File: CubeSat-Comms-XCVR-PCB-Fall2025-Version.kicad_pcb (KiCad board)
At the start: 4 copper layers, 93.9 x 97.3 mm, 70 parts, among them J1 Conn_01x02_Pin, J2 Conn_01x02_Pin, J3 Conn_Coaxial, J4 Conn_01x12_Pin, U1 CC1101RGP, U2 SKY65366-21, U3 PE4251MLI-Z, U4 NCP186AMX390TAG, Y1 NX3225GA-26MHZ-TI

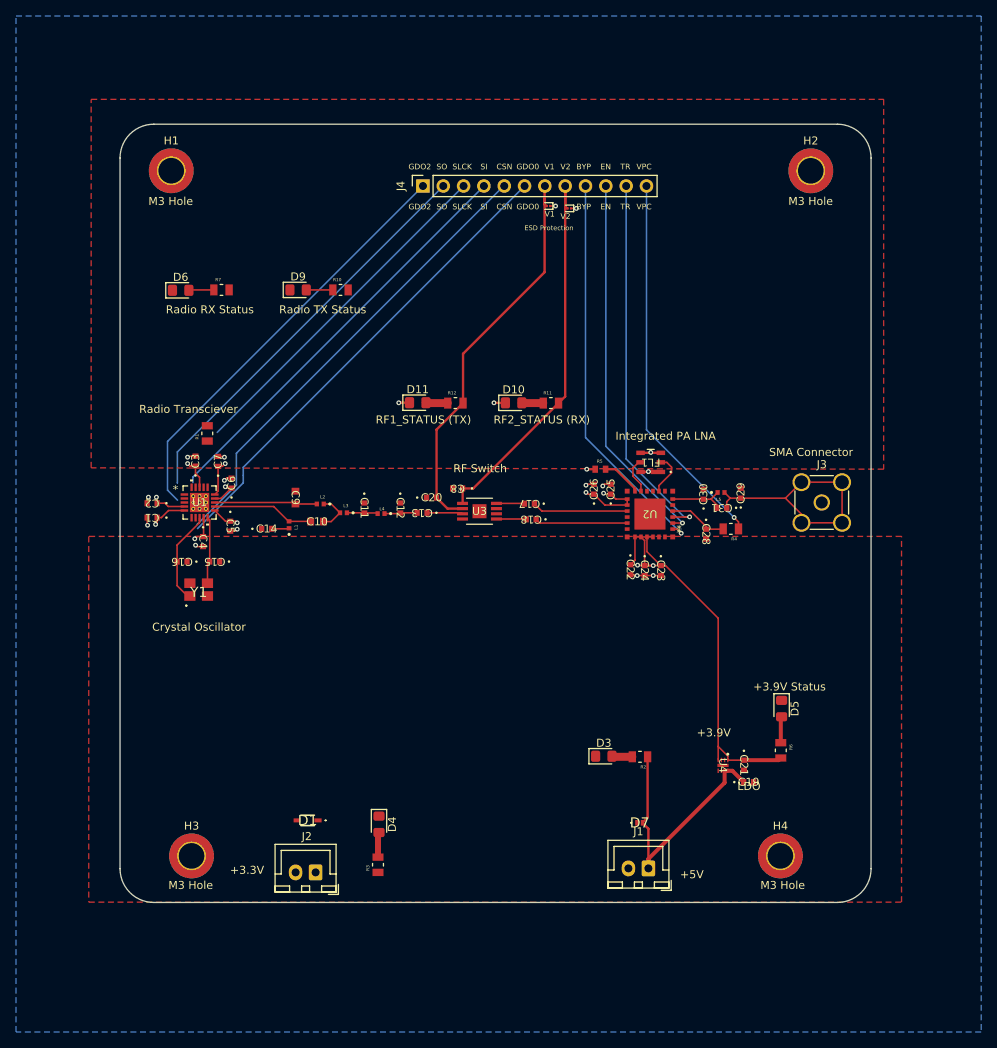
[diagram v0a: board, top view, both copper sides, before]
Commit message: pcb edits: sticking vias, trace routing...
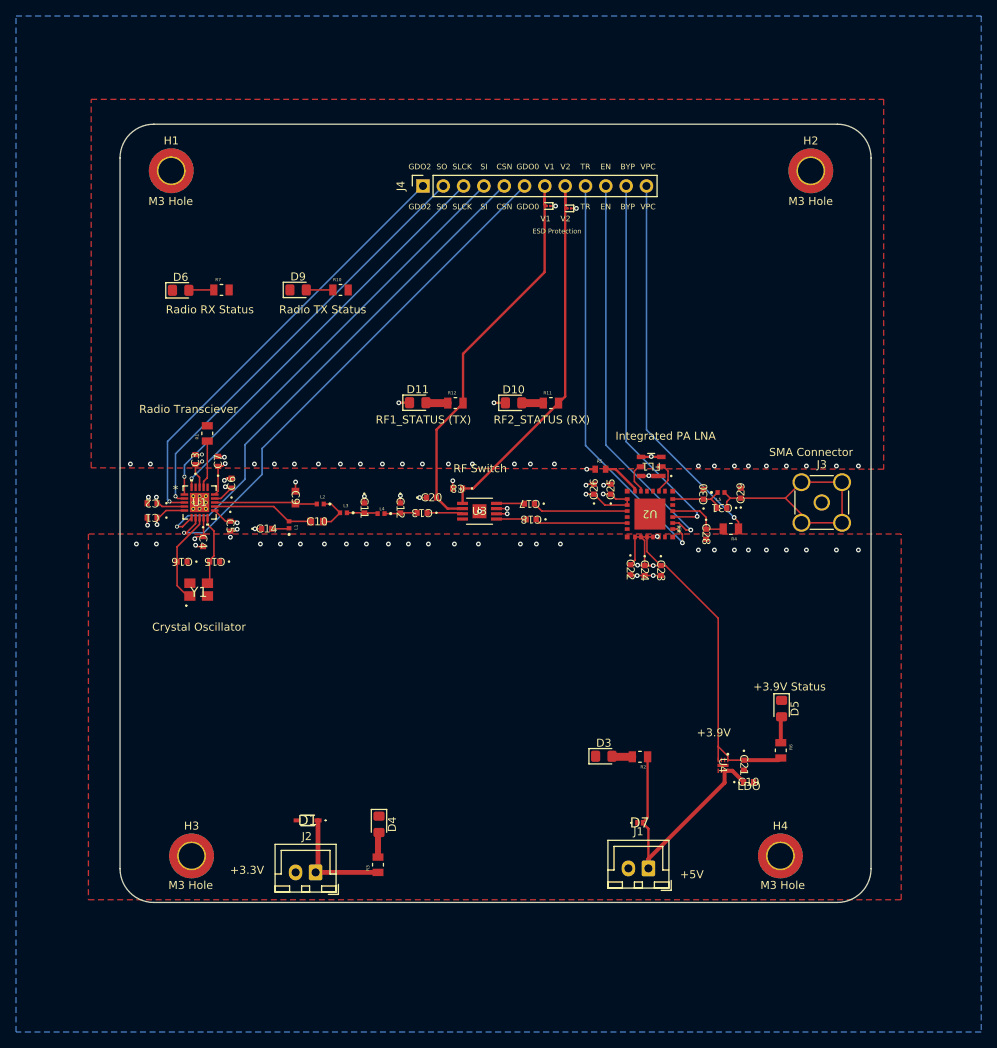
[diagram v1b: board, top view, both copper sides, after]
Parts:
- moved FL1 0.51 mm to (123.8, 88.1)
- moved C3 0.20 mm to (66.9, 87.2)
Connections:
- J4 pad 5: CSN -> GD00
- J4 pad 6: GD00 -> CSN
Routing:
- net +3.3V: track 38.0 -> 52.7 mm
- net SCLK: track 43.6 -> 53.0 mm, vias 0 -> 1
- net GND: track 22.6 -> 30.6 mm, vias 18 -> 79
- net CSN: track 58.3 -> 65.1 mm, vias 0 -> 1
- net Net-(U1-RBIAS): track 0.00 -> 5.98 mm
- net GD00: track 59.8 -> 63.4 mm, vias 0 -> 1
- net SO: track 50.9 -> 53.9 mm, vias 0 -> 1
- net EN: track 47.3 -> 50.0 mm
- net TR: track 49.6 -> 52.2 mm
- net GD02: track 53.0 -> 54.7 mm, vias 0 -> 1
- net SAW_IN: track 5.25 -> 4.05 mm
- net BYP: track 47.2 -> 48.1 mm
- net Net-(U2-VPC): track 7.46 -> 8.14 mm
- net SI: track 52.1 -> 52.8 mm, vias 0 -> 1
- net SAW_OUT: track 4.56 -> 3.92 mm

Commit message: revised board clearance rules, drc, routing, placements. TODO = redundant xcvr, impedance matching
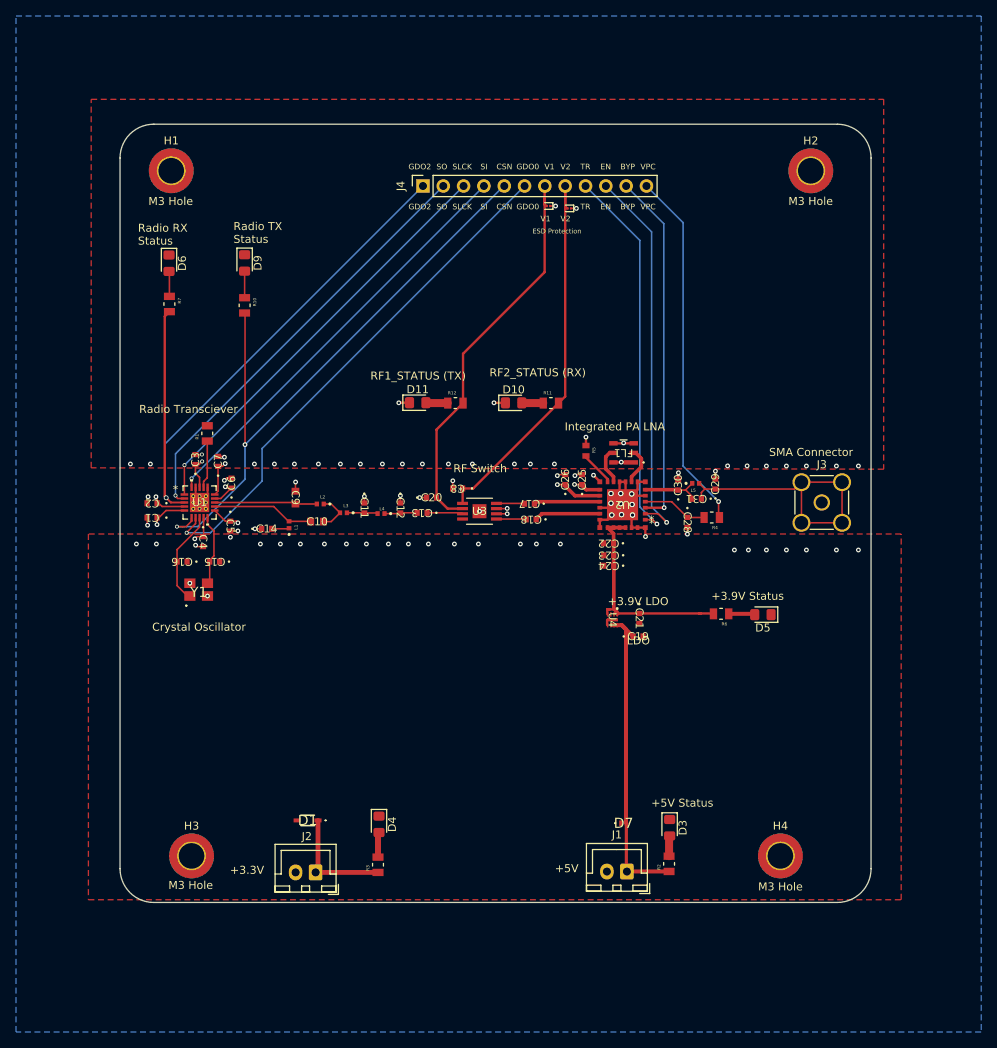
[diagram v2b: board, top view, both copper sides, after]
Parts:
- moved C19 22.9 mm to (122.2, 109.3)
- moved U4 22.9 mm to (119.0, 107.2)
- moved C21 22.5 mm to (122.4, 107.1)
- moved R6 18.6 mm to (132.6, 106.5), turned to 180 degrees
- moved R2 13.9 mm to (126.1, 137.7), turned to 90 degrees
- moved R10 12.1 mm to (73.0, 67.9), turned to -90 degrees
- moved D3 12.1 mm to (126.2, 133.2), turned to -90 degrees
- moved D5 12.0 mm to (137.8, 106.6), turned to 180 degrees
- moved D9 7.49 mm to (73.0, 62.6), turned to -90 degrees
- moved C23 6.79 mm to (118.5, 99.2), turned to 180 degrees
- moved R7 6.74 mm to (63.6, 67.8), turned to -90 degrees
- moved C24 4.52 mm to (118.5, 100.5), turned to 180 degrees
- moved C22 4.28 mm to (118.5, 97.7), turned to 180 degrees
- moved FL1 3.85 mm to (120.4, 86.4)
- moved C25 3.78 mm to (115.2, 89.7)
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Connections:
- U1 pad V: (no net) -> GND
- U4 pad 2: unconnected-(U4-OUT-Pad2) -> +3.9V
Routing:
- net GND: track 30.6 -> 64.9 mm, vias 79 -> 88
- net +3.9V: track 55.5 -> 28.8 mm, vias 2 -> 0
- net GD02: track 54.7 -> 78.5 mm
- net GD00: track 63.4 -> 80.2 mm, vias 1 -> 2
- net +5V: track 34.4 -> 39.6 mm
- net TR: track 52.2 -> 47.6 mm
- net Net-(J3-Ext): track 31.3 -> 35.1 mm
- net RX0: track 12.0 -> 8.27 mm
- net BYP: track 48.1 -> 44.5 mm
- net TX: track 11.6 -> 8.24 mm
- net VPC: track 47.6 -> 45.2 mm
- net EN: track 50.0 -> 48.3 mm
- net SAW_OUT: track 3.92 -> 4.69 mm
- net Net-(U2-RBIAS): track 5.00 -> 4.35 mm
- net SAW_IN: track 4.05 -> 4.67 mm
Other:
- rule pad_to_mask_clearance: 0 -> 0.2
- board text added: "+3.9V LDO"
- board text added: "+5V Status"
- board text removed: "+3.9V"

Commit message: editted silk screen and note on schematic about via tenting for CC1101 epad vias
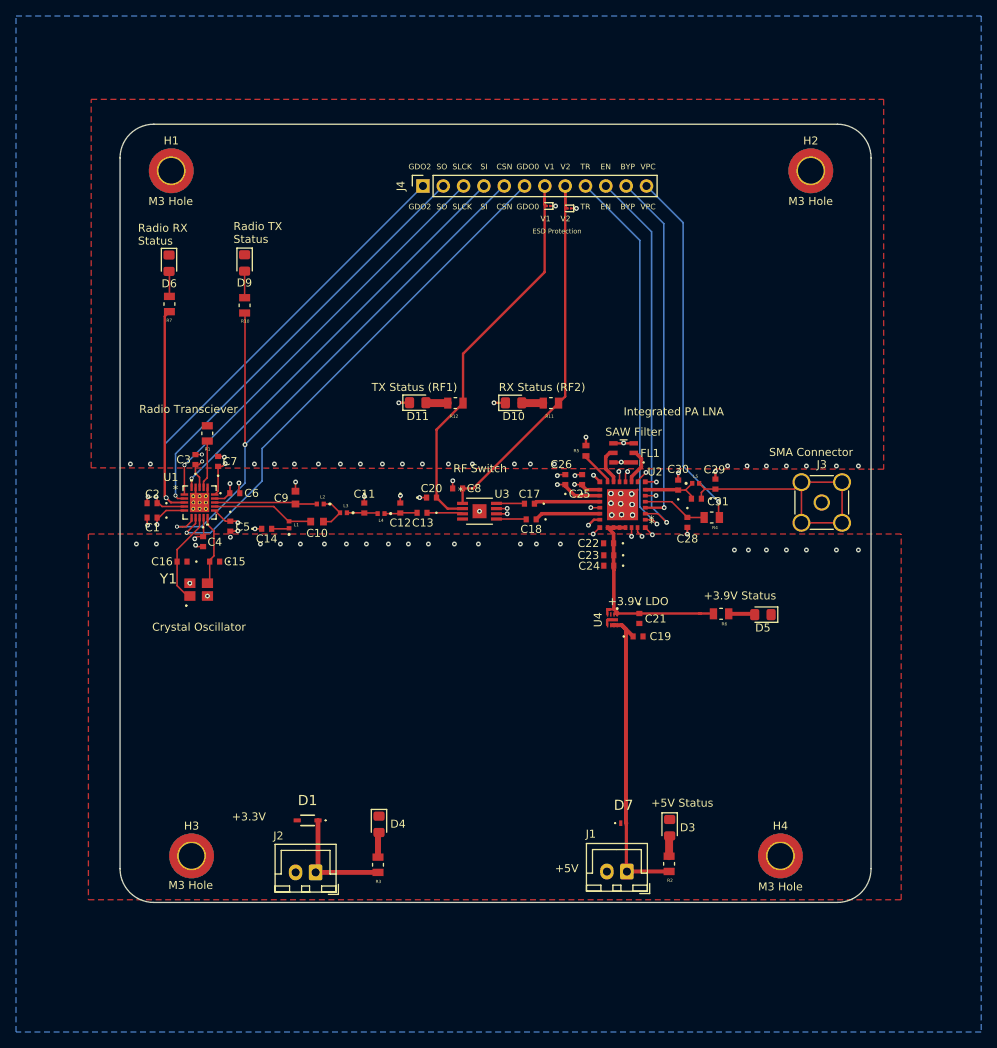
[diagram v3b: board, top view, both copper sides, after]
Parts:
- moved C6 1.32 mm to (71.8, 91.4), turned to 0 degrees
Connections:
- U1 pad V: GND -> (no net)
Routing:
- net GND: track 64.9 -> 54.7 mm, vias 88 -> 98
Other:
- board text added: "RX Status (RF2)"
- board text added: "SAW Filter"
- board text added: "TX Status (RF1)"
- board text removed: "LDO"
- board text removed: "RF1_STATUS (TX)"
- board text removed: "RF2_STATUS (RX)"

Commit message: test points and silkscreen
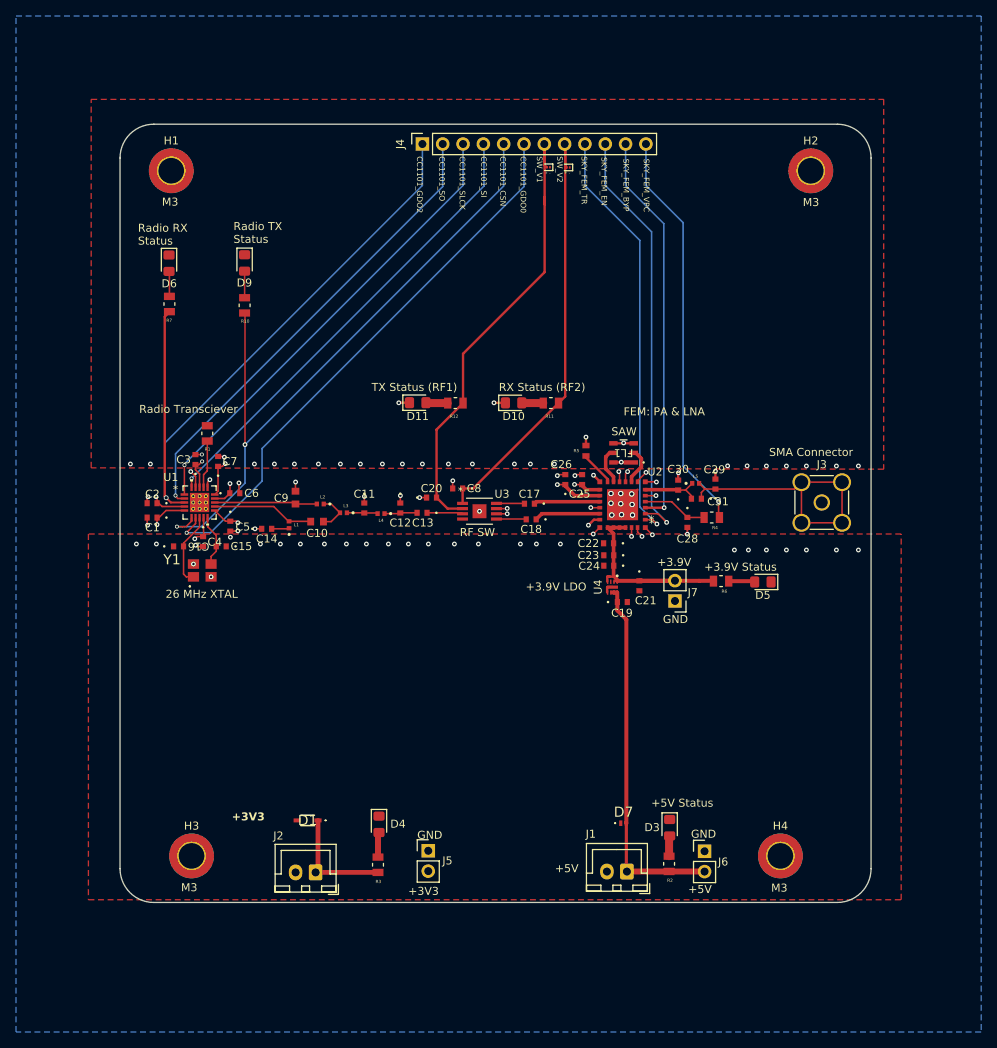
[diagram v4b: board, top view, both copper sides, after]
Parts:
- added J5: Conn_01x02_Pin, Connector_PinHeader_2.54mm:PinHeader_1x02_P2.54mm_Vertical, F.Cu at (96.0, 136.1)
- added J6: Conn_01x02_Pin, Connector_PinHeader_2.54mm:PinHeader_1x02_P2.54mm_Vertical, F.Cu at (130.5, 136.2)
- added J7: Conn_01x02_Pin, Connector_PinHeader_2.54mm:PinHeader_1x02_P2.54mm_Vertical, F.Cu at (126.8, 104.9)
- moved J4 5.25 mm to (95.2, 47.8)
- moved D8 5.12 mm to (113.5, 50.7)
- moved D2 4.84 mm to (111.0, 50.7)
- moved C19 4.73 mm to (120.2, 105.0)
- moved C21 4.08 mm to (122.4, 103.0)
- moved D5 4.08 mm to (137.8, 102.5)
- moved U4 4.08 mm to (119.0, 103.1)
- moved R6 4.08 mm to (132.6, 102.4)
- moved Y1 2.44 mm to (67.7, 101.1)
- moved C15 2.07 mm to (70.1, 98.0)
- moved C16 1.96 mm to (64.8, 98.0), turned to 0 degrees
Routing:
- net V1: track 49.6 -> 57.5 mm
- net +5V: track 39.6 -> 45.8 mm
- net V2: track 48.7 -> 54.0 mm
- net SI: track 52.8 -> 58.1 mm
- net VPC: track 45.2 -> 50.5 mm
- net TR: track 47.6 -> 52.9 mm
- net BYP: track 44.5 -> 49.8 mm
- net EN: track 48.3 -> 53.6 mm
- net GD02: track 78.5 -> 83.7 mm
- net SO: track 53.9 -> 59.1 mm
- net CSN: track 64.9 -> 70.1 mm
- net SCLK: track 53.0 -> 58.2 mm
- net GD00: track 80.4 -> 85.6 mm
- net GND: track 54.7 -> 52.2 mm
- net /XOSC_Q1: track 11.8 -> 9.26 mm
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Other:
- board text added: "+"
- board text added: "+3.9V"
- board text added: "+3V3"
- board text added: "-"
- board text added: "26 MHz XTAL"
- board text added: "CC1101_CSN"
- board text added: "CC1101_GDO0"
- board text added: "CC1101_GDO2"
- board text added: "CC1101_SI"
- board text added: "CC1101_SLCK"
- board text added: "CC1101_SO"
- board text added: "FEM: PA & LNA"
- board text added: "GND"
- board text added: "Jonathan Lin Fall 2025"
- board text added: "M3"
- board text added: "RF SW"
- board text added: "SAW"
- board text added: "SKY_FEM_BYP"
- board text added: "SKY_FEM_EN"
- board text added: "SKY_FEM_TR"
- board text added: "SKY_FEM_VPC"
- board text added: "SW_V1"
- board text added: "SW_V2"
- board text removed: "+3.3V"
- board text removed: "BYP"
- board text removed: "CSN"
- board text removed: "Crystal Oscillator"
- board text removed: "EN"
- board text removed: "ESD Protection"
- board text removed: "GDO0"
- board text removed: "GDO2"
- board text removed: "Integrated PA LNA"
- board text removed: "M3 Hole"
- board text removed: "RF Switch"
- board text removed: "SAW Filter"
- board text removed: "SI"
- board text removed: "SLCK"
- board text removed: "SO"
- board text removed: "TR"
- board text removed: "V1"
- board text removed: "V2"
- board text removed: "VPC"

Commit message: added external signal injecting capability
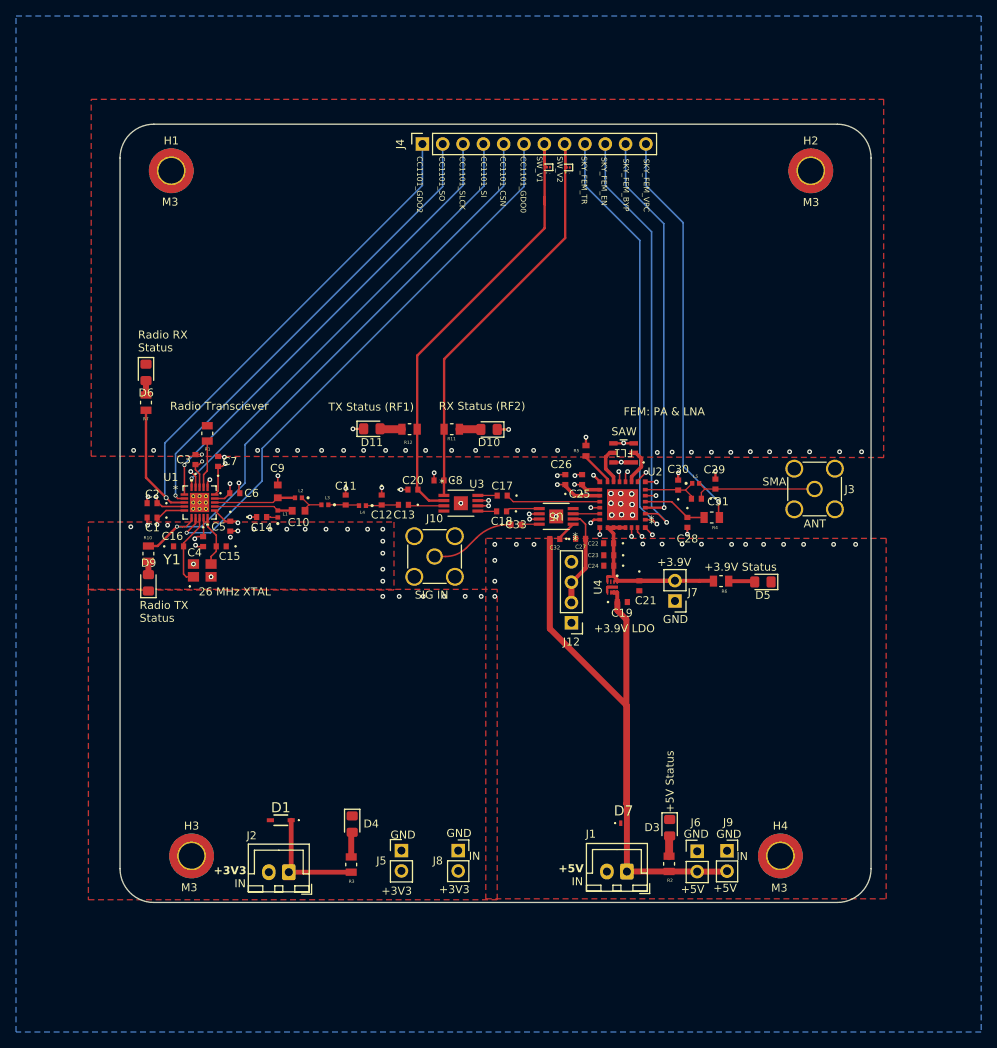
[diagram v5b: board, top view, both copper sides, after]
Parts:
- added C27: 220pF, comms-board-footprints-passives:G-188_MUR-L-100nF-GRM188, F.Cu at (115.0, 97.1)
- added C32: 220pF, comms-board-footprints-passives:G-188_MUR-L-100nF-GRM188, F.Cu at (111.8, 97.1)
- added C33: 68pF, comms-board-footprints-passives:G-188_MUR-L-100nF-GRM188, F.Cu at (107.0, 95.3)
- added J10: Conn_Coaxial, Connector_Coaxial:SMA_Amphenol_132134-11_Vertical, F.Cu at (96.8, 99.3)
- added J12: Conn_01x04_Pin, Connector_PinHeader_2.54mm:PinHeader_1x04_P2.54mm_Vertical, F.Cu at (113.9, 107.6)
- added J8: Conn_01x02_Pin, Connector_PinSocket_2.54mm:PinSocket_1x02_P2.54mm_Vertical, F.Cu at (99.7, 136.1)
- added J9: Conn_01x02_Pin, Connector_PinSocket_2.54mm:PinSocket_1x02_P2.54mm_Vertical, F.Cu at (133.3, 136.1)
- added U5: PE4251MLI-Z, comms-board-footprints:8-MSOP_PE4251_PSM, F.Cu at (112.0, 94.3)
- moved D9 41.7 mm to (61.0, 102.6), turned to 90 degrees
- moved R10 33.3 mm to (61.0, 99.0), turned to 90 degrees
- moved D6 13.9 mm to (60.7, 76.3)
- moved R11 12.8 mm to (98.9, 83.4), turned to 180 degrees
- moved R7 12.7 mm to (60.7, 80.1)
- moved R12 6.59 mm to (93.6, 83.4)
- moved D11 6.59 mm to (88.9, 83.3)
- moved D10 4.53 mm to (103.6, 83.4), turned to 180 degrees
- moved C18 3.83 mm to (105.2, 93.7)
- moved C17 3.55 mm to (105.2, 91.7)
- moved D1 3.35 mm to (77.5, 132.3)
- moved D4 3.35 mm to (86.5, 132.8)
- moved J2 3.35 mm to (78.5, 138.8)
- moved J5 3.35 mm to (92.6, 136.1)
- moved R3 3.35 mm to (86.3, 137.8)
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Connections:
- C18 pad 1: TX -> TX_JUMP
- C29 pad 1: Net-(J3-Ext) -> Net-(J3-In)
- C31 pad 1: Net-(J3-Ext) -> Net-(J3-In)
- J3 pad 1: GND -> Net-(J3-In)
- J3 pad 2: Net-(J3-Ext) -> GND
- L5 pad 1: Net-(J3-Ext) -> Net-(J3-In)
- U1 pad V: (no net) -> GND
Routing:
- net +5V: track 45.8 -> 91.9 mm
- net Net-(J3-Ext): track 35.1 -> 0.00 mm
- net Net-(J3-In): track 0.00 -> 16.1 mm
- net TX_SEL: track 0.00 -> 12.4 mm
- net GD00: track 85.6 -> 73.7 mm, vias 2 -> 1
- net GD02: track 83.7 -> 72.1 mm
- net Net-(J10-In): track 0.00 -> 10.8 mm
- net TX: track 8.24 -> 3.33 mm
- net TX_JUMP: track 0.00 -> 4.22 mm
- net RX0: track 8.27 -> 11.9 mm
- net RF_P: track 12.8 -> 9.90 mm
- net RF_N: track 12.8 -> 10.3 mm
- net Net-(U5-V2): track 0.00 -> 2.54 mm
- net Net-(U5-RF2): track 0.00 -> 2.30 mm
- net Net-(D9-A): track 3.32 -> 1.67 mm
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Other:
- board text added: "ANT"
- board text added: "IN"
- board text added: "SIG IN"
- board text added: "SMA"
- board text removed: "RF SW"
- board text removed: "SMA Connector"
